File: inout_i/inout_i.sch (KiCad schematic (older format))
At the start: 1 part, among them P1 DIN_41612_128P

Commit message: Added and tied in Inout VI. Pulled in all PIPA related things. Almost there!
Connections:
- net CH1213: now also P1.47 (15B); no longer P1.44 (12B)
- net CH1214: now also P1.48 (16B); no longer P1.45 (13B)
- net GND: no longer P1.46 (14B), P1.47 (15B), P1.48 (16B)
- net TMPOUT: now also P1.46 (14B); no longer P1.43 (11B)
- new net CCH12: P1.43 (11B)
- new net RCH12/: P1.44 (12B)
- new net WCH12/: P1.45 (13B)
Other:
- moved on the sheet: P1A, P1B, P1C, P1D, P1E, P1F

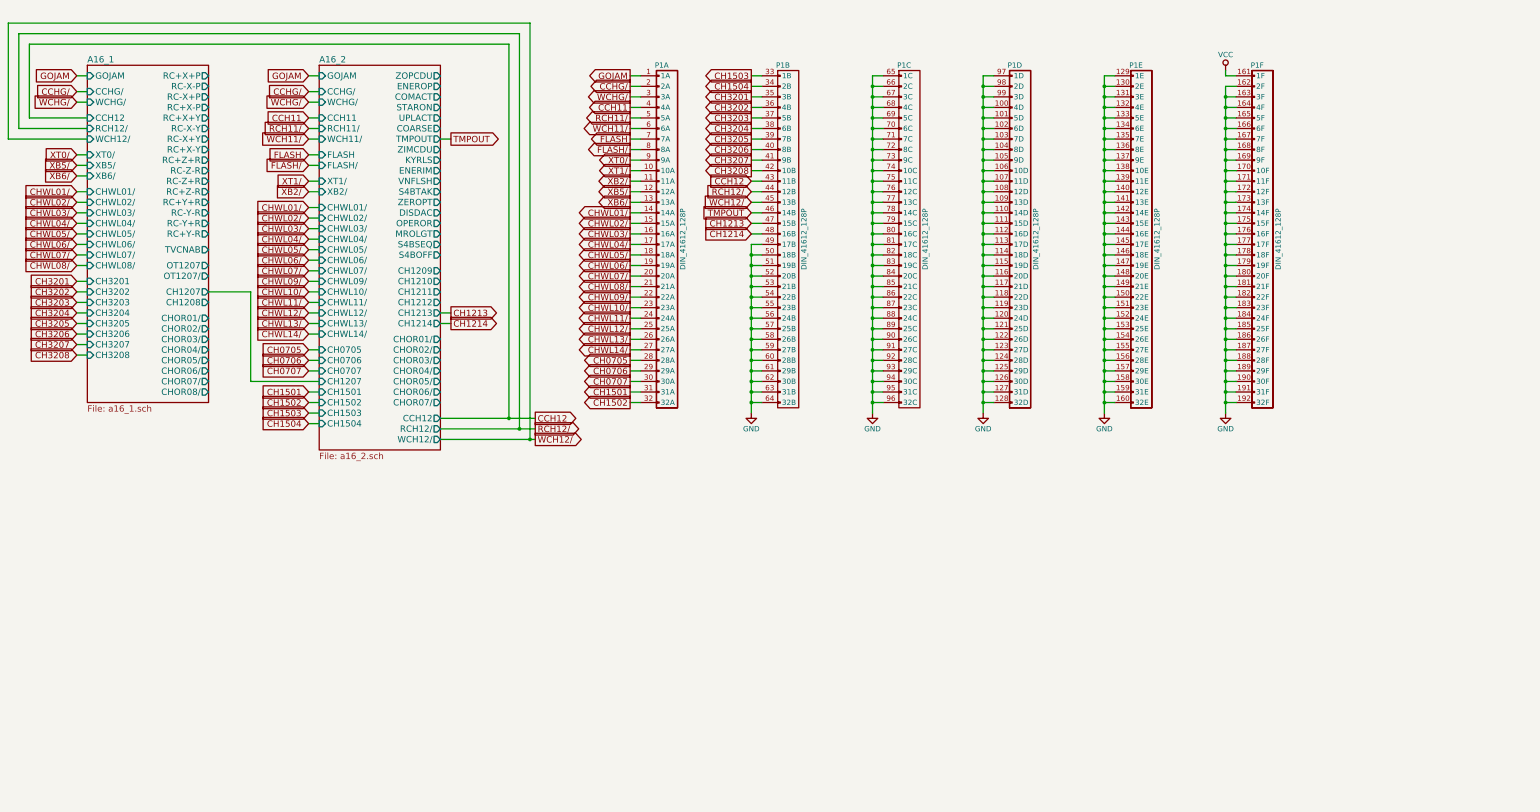
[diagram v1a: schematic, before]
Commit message: Added and tied in Inout VII, the final logic module!
I still need to comb through the schematics to see if there are any
stray gates I missed. The initial conditions are also pretty much
guaranteed to be wrong. But it's mostly all there!
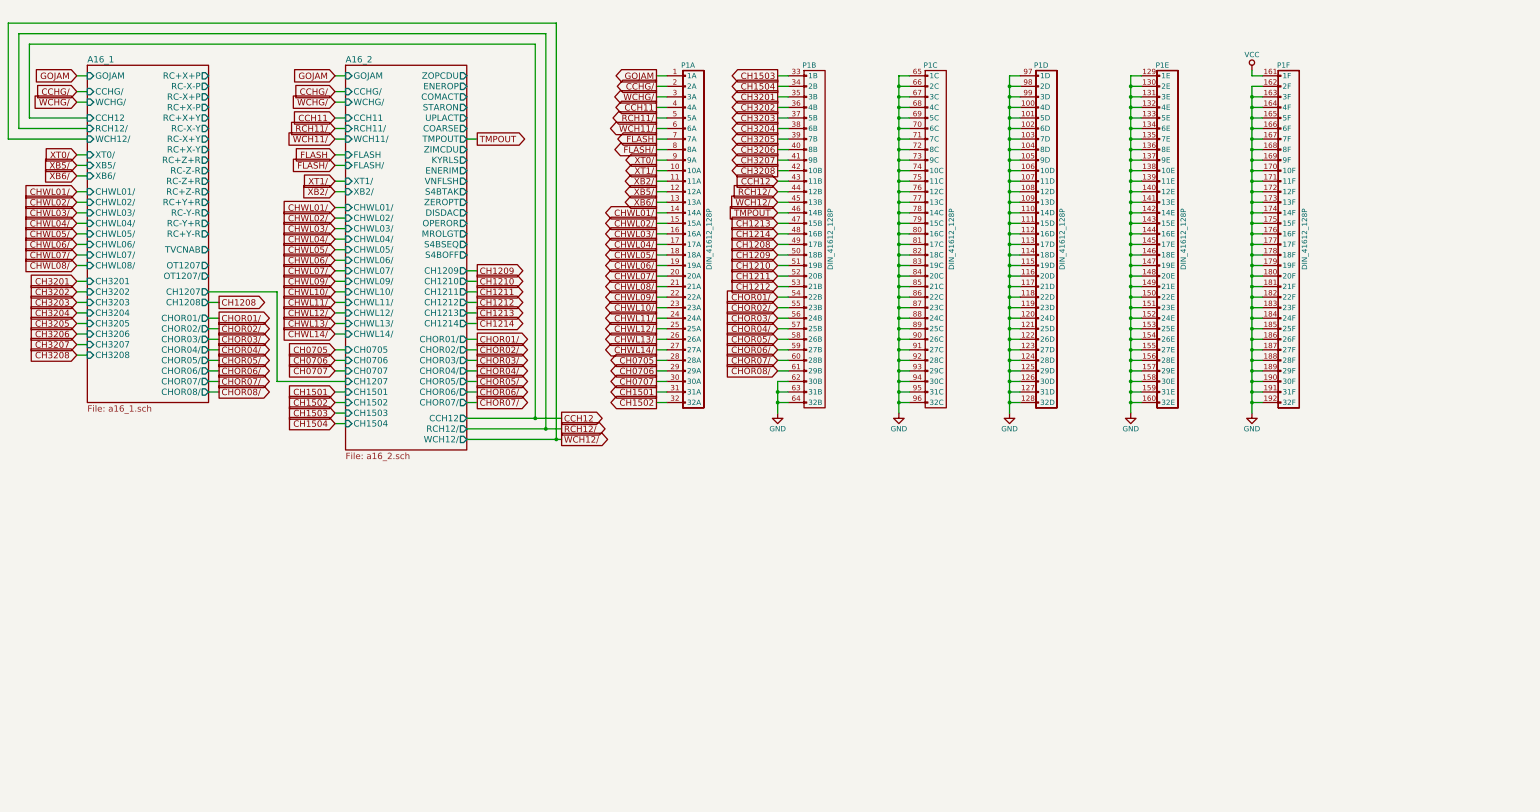
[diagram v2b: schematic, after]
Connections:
- net GND: no longer P1.49 (17B), P1.50 (18B), P1.51 (19B), P1.52 (20B), P1.53 (21B), P1.54 (22B), P1.55 (23B), P1.56 (24B), P1.57 (25B), P1.58 (26B), P1.59 (27B), P1.60 (28B), P1.61 (29B)
- new net CH1208: P1.49 (17B)
- new net CH1209: P1.50 (18B)
- new net CH1210: P1.51 (19B)
- new net CH1211: P1.52 (20B)
- new net CH1212: P1.53 (21B)
- new net CHOR01/: P1.54 (22B)
- new net CHOR02/: P1.55 (23B)
- new net CHOR03/: P1.56 (24B)
- new net CHOR04/: P1.57 (25B)
- new net CHOR05/: P1.58 (26B)
- new net CHOR06/: P1.59 (27B)
- new net CHOR07/: P1.60 (28B)
- new net CHOR08/: P1.61 (29B)
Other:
- moved on the sheet: P1A, P1B, P1C, P1D, P1E, P1F

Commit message: Broke out most (all?) of the DSKY outputs
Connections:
- net GND: no longer P1.62 (30B), P1.63 (31B), P1.64 (32B), P1.65 (1C), P1.66 (2C)
- new net COMACT: P1.62 (30B)
- new net KYRLS: P1.64 (32B)
- new net OPEROR: P1.66 (2C)
- new net UPLACT: P1.63 (31B)
- new net VNFLSH: P1.65 (1C)
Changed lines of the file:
@@
 $EndComp
 Wire Wire Line
-	9250 1500 9150 1500
-Connection ~ 9150 1500
-Wire Wire Line
 	9150 1600 9250 1600
-Connection ~ 9150 1600
 Wire Wire Line
 	9150 1700 9250 1700
@@
 	9150 4500 9250 4500
 Connection ~ 9150 4500
-Wire Wire Line
-	9250 1400 9150 1400
-Wire Wire Line
-	9150 1400 9150 4600
 $Comp
 L GND #PWR01
@@
 $EndComp
 $Sheet
-S 3900 1300 1150 3650
+S 3900 1300 1150 3800
 U 572139C1
 F0 "A16_2" 60
@@
 F65 "CCH12" O R 5050 4650 60
 F66 "RCH12/" O R 5050 4750 60
+F67 "ISSWAR" O R 5050 5000 60
 $EndSheet
 Text GLabel 1350 1400 0    60   Input ~ 0
@@
 CHOR07/
 Wire Wire Line
-	8000 4300 8100 4300
-Wire Wire Line
-	8000 4400 8100 4400
-Connection ~ 8000 4400
-Wire Wire Line
-	8000 4500 8100 4500
-Connection ~ 8000 4500
-Wire Wire Line
-	8000 4300 8000 4600
-$Comp
-L GND #PWR06
-U 1 1 572CC374
-P 8000 4600
-F 0 "#PWR06" H 8000 4350 50  0001 C CNN
-F 1 "GND" H 8000 4450 50  0000 C CNN
-F 2 "" H 8000 4600 60  0000 C CNN
-F 3 "" H 8000 4600 60  0000 C CNN
-	1    8000 4600
-	1    0    0    -1
-$EndComp
+	5050 1600 5150 1600
+Text GLabel 5150 1600 2    60   Output ~ 0
+COMACT
+Wire Wire Line
+	8100 4300 8000 4300
+Text GLabel 8000 4300 0    60   Input ~ 0
+COMACT
+Wire Wire Line
+	5050 1800 5150 1800
+Text GLabel 5150 1800 2    60   Output ~ 0
+UPLACT
+Wire Wire Line
+	8100 4400 8000 4400
+Text GLabel 8000 4400 0    60   Input ~ 0
+UPLACT
+Wire Wire Line
+	5050 2200 5150 2200
+Text GLabel 5150 2200 2    60   Output ~ 0
+KYRLS
+Wire Wire Line
+	8100 4500 8000 4500
+Text GLabel 8000 4500 0    60   Input ~ 0
+KYRLS
+Wire Wire Line
+	5050 2400 5150 2400
+Text GLabel 5150 2400 2    60   Output ~ 0
+VNFLSH
+Wire Wire Line
+	9250 1400 9150 1400
+Text GLabel 9150 1400 0    60   Input ~ 0
+VNFLSH
+Wire Wire Line
+	5050 2800 5150 2800
+Text GLabel 5150 2800 2    60   Output ~ 0
+OPEROR
+Wire Wire Line
+	9250 1500 9150 1500
+Text GLabel 9150 1500 0    60   Input ~ 0
+OPEROR
+Wire Wire Line
+	9150 1600 9150 4600
 $EndSCHEMATC

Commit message: Updated Inout I to be on +4VSW
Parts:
- added U16001, U16005, U16006, U16007, U16008, U16009, U16010, U16013, U16014, U16015, U16016, U16017, U16018, U16022, U16023, U16024, U16027, U16028, U16029, U16031, U16033, U16034, U16035, U16036, U16037, U16039, U16040, U16042, U16043, U16045, U16046, U16047, U16048, U16049, U16051, U16052, U16054, U16055, U16056, U16058: 74HC02, symbol 74HC02
- added U16002, U16011, U16019, U16026, U16030, U16038, U16050, U16057: 74HC04, symbol 74HC04
- added U16003, U16012, U16020, U16025, U16032, U16041, U16053: 74HC27, symbol 74HC27
- added U16004, U16021, U16044: 74LVC07, symbol 74LVC07
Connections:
- net labels added: +4VSW
- net labels removed: VCC
- wire segments 295 -> 307
